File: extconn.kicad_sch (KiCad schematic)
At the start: 24 parts, among them J1401 Conn_02x10_Odd_Even, U1401 74AVC4T245PW, U1402 74AVC4T245PW

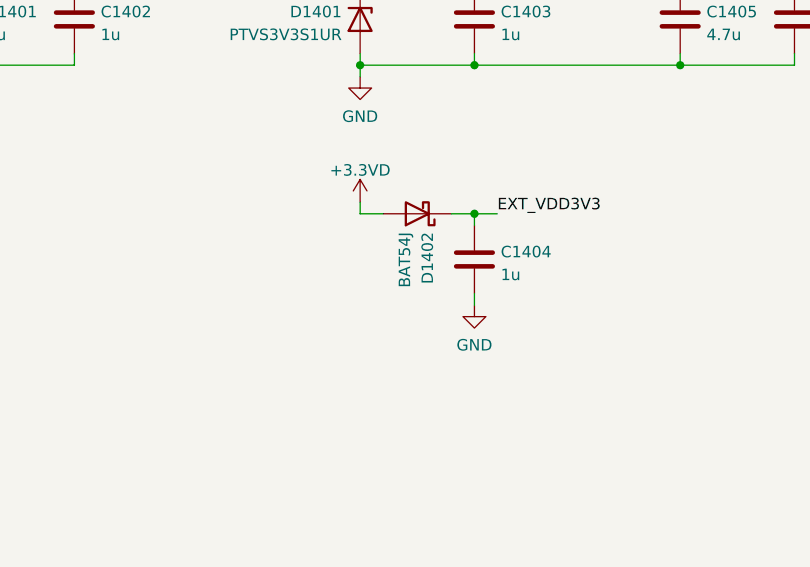
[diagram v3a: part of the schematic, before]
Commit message: Fix: correct BAT54 PN and package - SOD323 not SOD323F
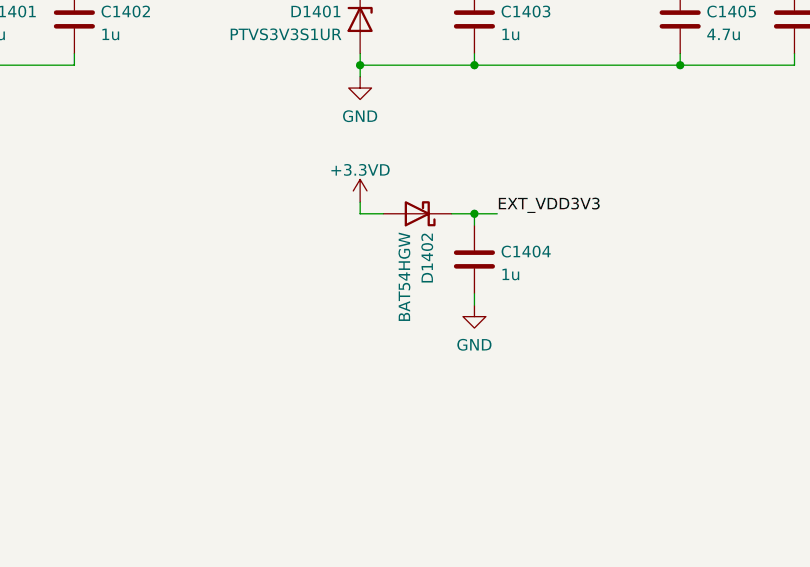
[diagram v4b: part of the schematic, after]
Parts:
- D1402: value BAT54J -> BAT54HGW; footprint Diode_SMD:D_SOD-323F -> Diode_SMD:D_SOD-323
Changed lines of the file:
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@@
       (effects (font (size 1.27 1.27)) (justify left))
     )
-    (property "Value" "BAT54J" (id 1) (at 208.1653 66.802 90)
+    (property "Value" "BAT54HGW" (id 1) (at 208.1653 66.802 90)
       (effects (font (size 1.27 1.27)) (justify left))
     )
-    (property "Footprint" "Diode_SMD:D_SOD-323F" (id 2) (at 209.55 60.325 0)
+    (property "Footprint" "Diode_SMD:D_SOD-323" (id 2) (at 209.55 60.325 0)
       (effects (font (size 1.27 1.27)) hide)
     )
